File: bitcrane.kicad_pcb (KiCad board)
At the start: 4 copper layers, 110 x 100 mm, 119 parts, among them J1 PSU Comm, J10 Hashboard2, J14 0353180420, J15 0353180420, J16 0353180420, J17 0353180420, J2 Hashboard0, J3 0455580003, J4 61900411021, J5 61900411021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

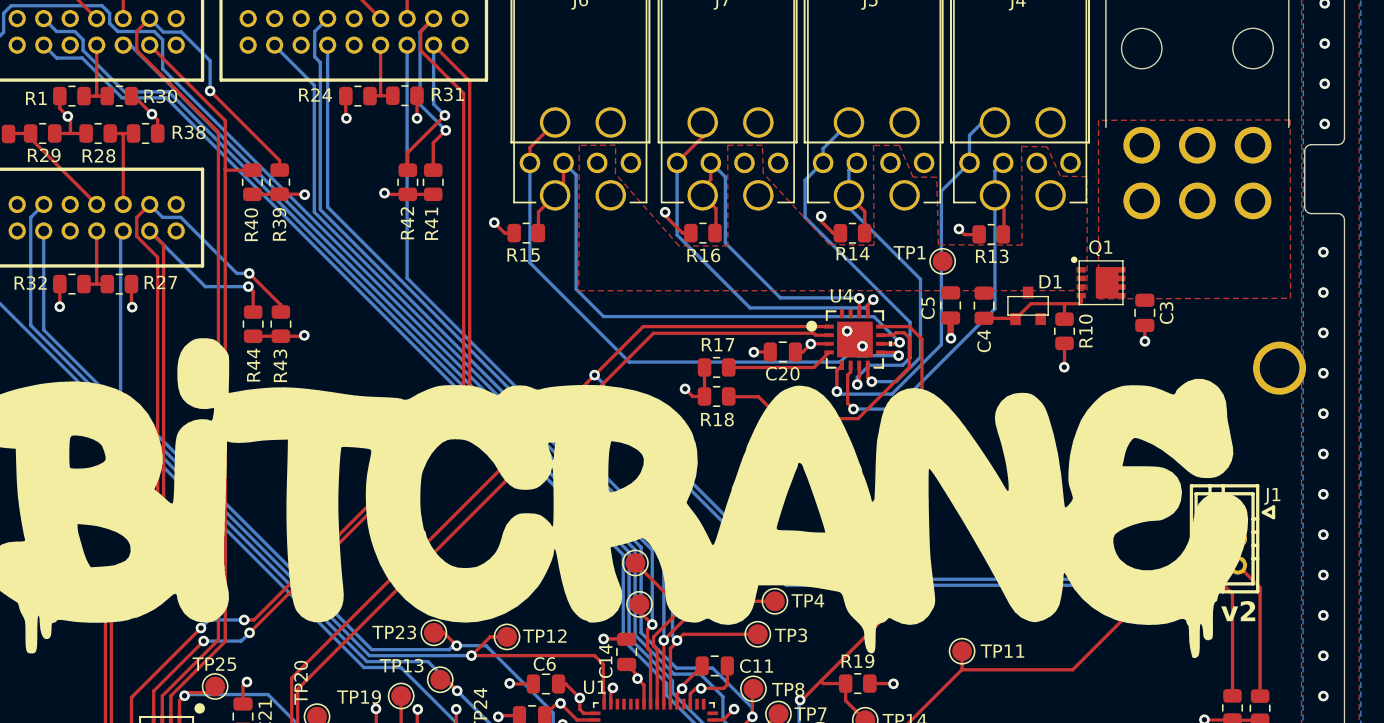
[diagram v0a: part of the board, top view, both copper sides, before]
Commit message: fix for #8. regenerated gerbers. bump version to 2.1
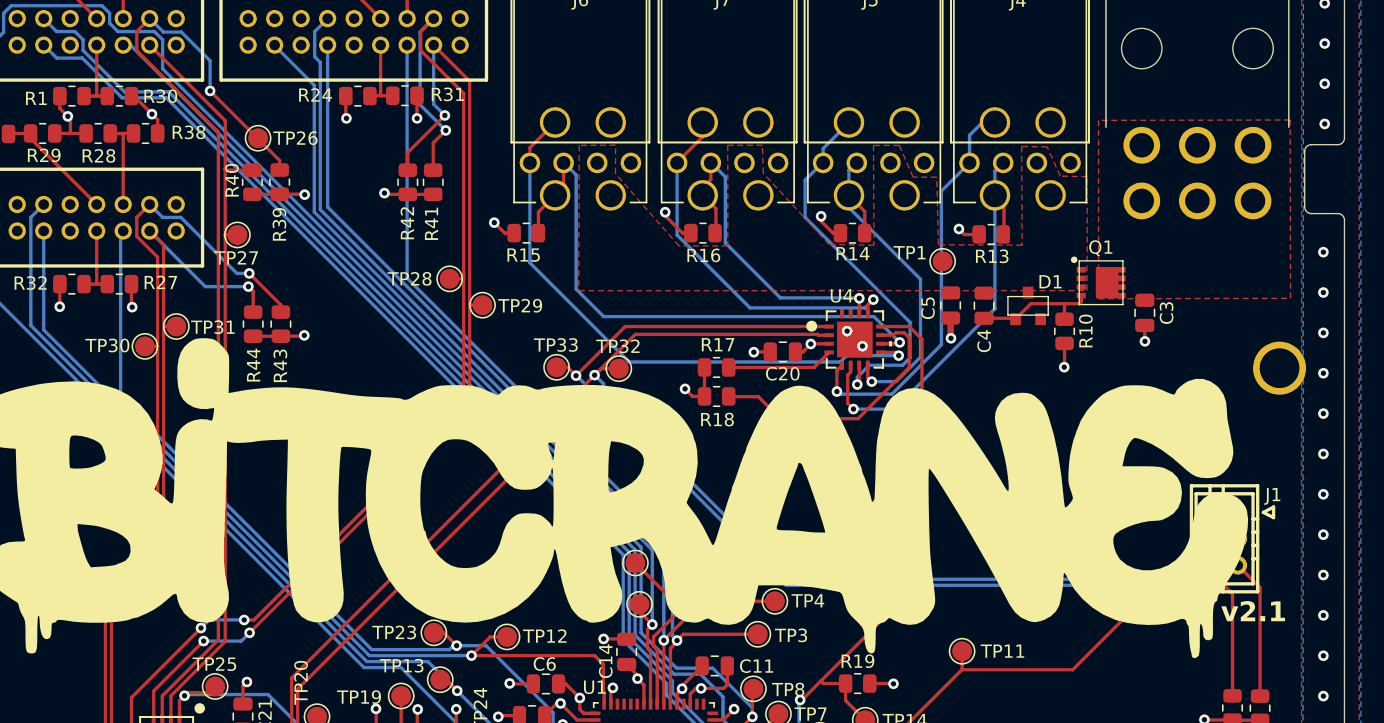
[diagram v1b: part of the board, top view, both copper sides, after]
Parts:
- added TP26: TestPoint, TestPoint:TestPoint_Pad_D1.5mm, F.Cu at (86.3, 50.0)
- added TP27: TestPoint, TestPoint:TestPoint_Pad_D1.5mm, F.Cu at (84.7, 57.3)
- added TP28: TestPoint, TestPoint:TestPoint_Pad_D1.5mm, F.Cu at (100.7, 60.6)
- added TP29: TestPoint, TestPoint:TestPoint_Pad_D1.5mm, F.Cu at (103.2, 62.6)
- added TP30: TestPoint, TestPoint:TestPoint_Pad_D1.5mm, F.Cu at (77.7, 65.7)
- added TP31: TestPoint, TestPoint:TestPoint_Pad_D1.5mm, F.Cu at (80.1, 64.2)
- added TP32: TestPoint, TestPoint:TestPoint_Pad_D1.5mm, F.Cu at (113.5, 67.4)
- added TP33: TestPoint, TestPoint:TestPoint_Pad_D1.5mm, F.Cu at (108.8, 67.3)
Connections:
- U4 pad 1: /SCL3 -> /SDA3
- U4 pad 2: /SDA3 -> /SCL3
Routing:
- net /SDA3: track 137.4 -> 142.0 mm, vias 1 -> 2
- net /SCL3: track 135.4 -> 137.3 mm
- net /SCL1: track 81.5 -> 82.6 mm
- net /SDA1: track 74.5 -> 75.5 mm
- net /SDA2: track 54.3 -> 55.2 mm
- net /SCL2: track 60.0 -> 61.0 mm
- net /SDA0: track 57.0 -> 58.0 mm
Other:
- board text added: "v2.1"
- board text removed: "v2"

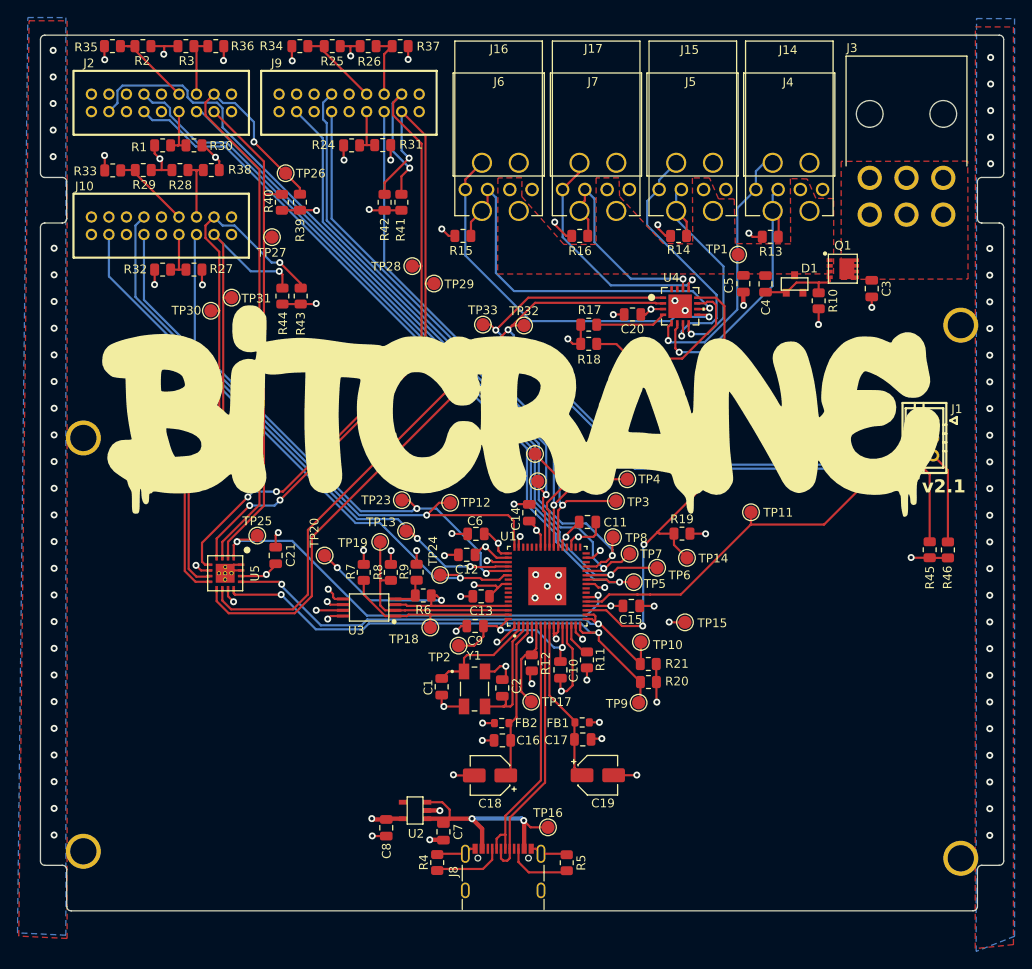
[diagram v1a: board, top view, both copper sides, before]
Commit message: fix for #9. regenerated gerbers. bumped version to 2.2
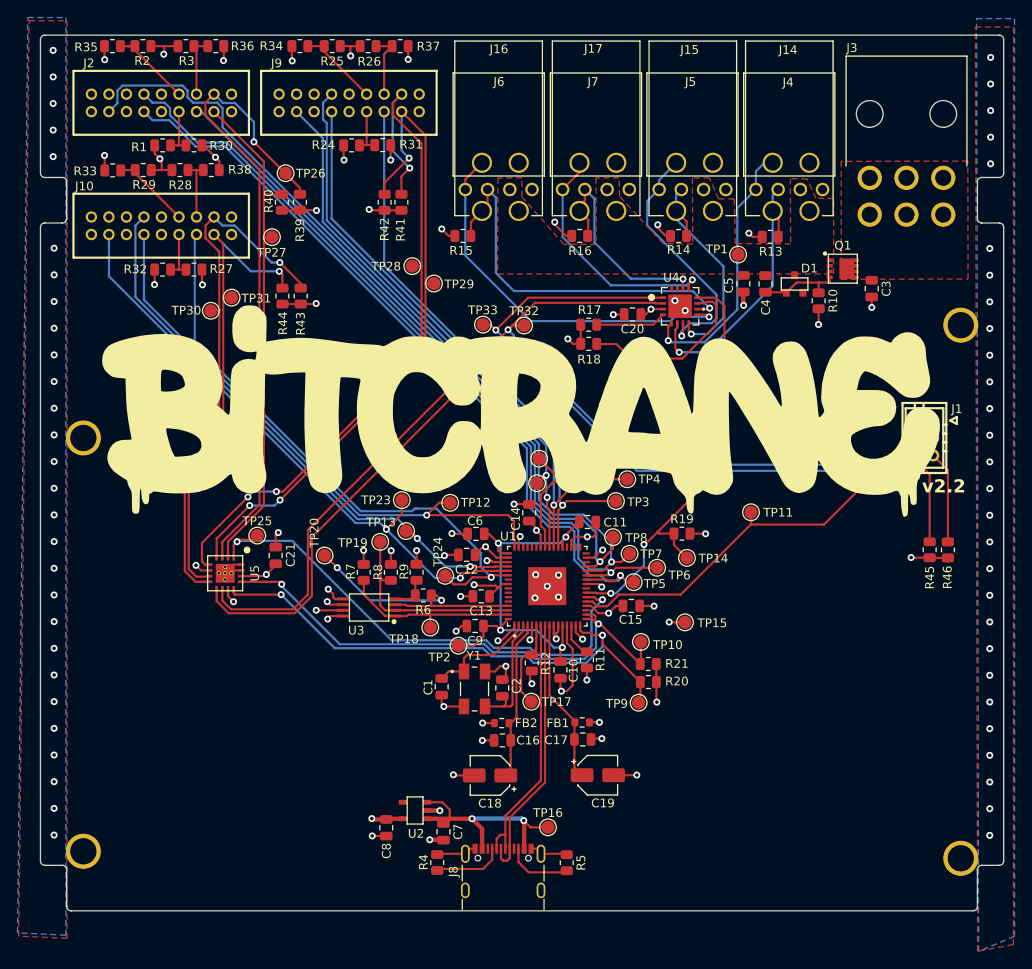
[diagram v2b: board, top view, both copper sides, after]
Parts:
- moved TP21 3.35 mm to (115.0, 85.4)
- moved TP22 2.58 mm to (115.2, 82.6)
- moved TP24 0.59 mm to (104.5, 96.0)
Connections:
- TP21 pad 1: /PLUG1 -> /RST1
- TP22 pad 1: /RST1 -> /PLUG1
- TP23 pad 1: /PLUG2 -> /RST2
- TP24 pad 1: /RST2 -> /PLUG2
- TP7 pad 1: /PLUG0 -> /RST0
- TP8 pad 1: /RST0 -> /PLUG0
- U1 pad 19: /FAN_ALERT -> unconnected-(U1-ADBUS3-Pad19)
- U1 pad 23: unconnected-(U1-ADBUS6-Pad23) -> /FAN_ALERT
- U1 pad 28: /PLUG0 -> /RST0
- U1 pad 29: /RST0 -> /PLUG0
- U1 pad 40: /PLUG1 -> /RST1
- U1 pad 41: /RST1 -> /PLUG1
- U1 pad 53: /PLUG2 -> /RST2
- U1 pad 54: /RST2 -> /PLUG2
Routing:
- net /RESET: track 52.4 -> 58.7 mm
- net /FAN_ALERT: track 56.5 -> 50.3 mm
- net /SDA: track 56.2 -> 60.4 mm
- net /PLUG2: track 62.8 -> 66.8 mm, vias 2 -> 1
- net /SCL: track 57.5 -> 60.9 mm
- net /TXD0: track 86.4 -> 88.8 mm
- net /RST2: track 67.4 -> 69.1 mm, vias 1 -> 2
- net /RXD0: track 89.3 -> 90.6 mm
- net /RST0: track 93.3 -> 94.6 mm
- net VCCIO: track 95.5 -> 96.5 mm
- net GND: track 107.1 -> 106.5 mm
- net /RST1: track 63.7 -> 63.4 mm, vias 1 -> 2
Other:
- board text added: "v2.2"
- board text removed: "v2.1"

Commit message: fix for #10 small DRC fixes. updated to v2.3
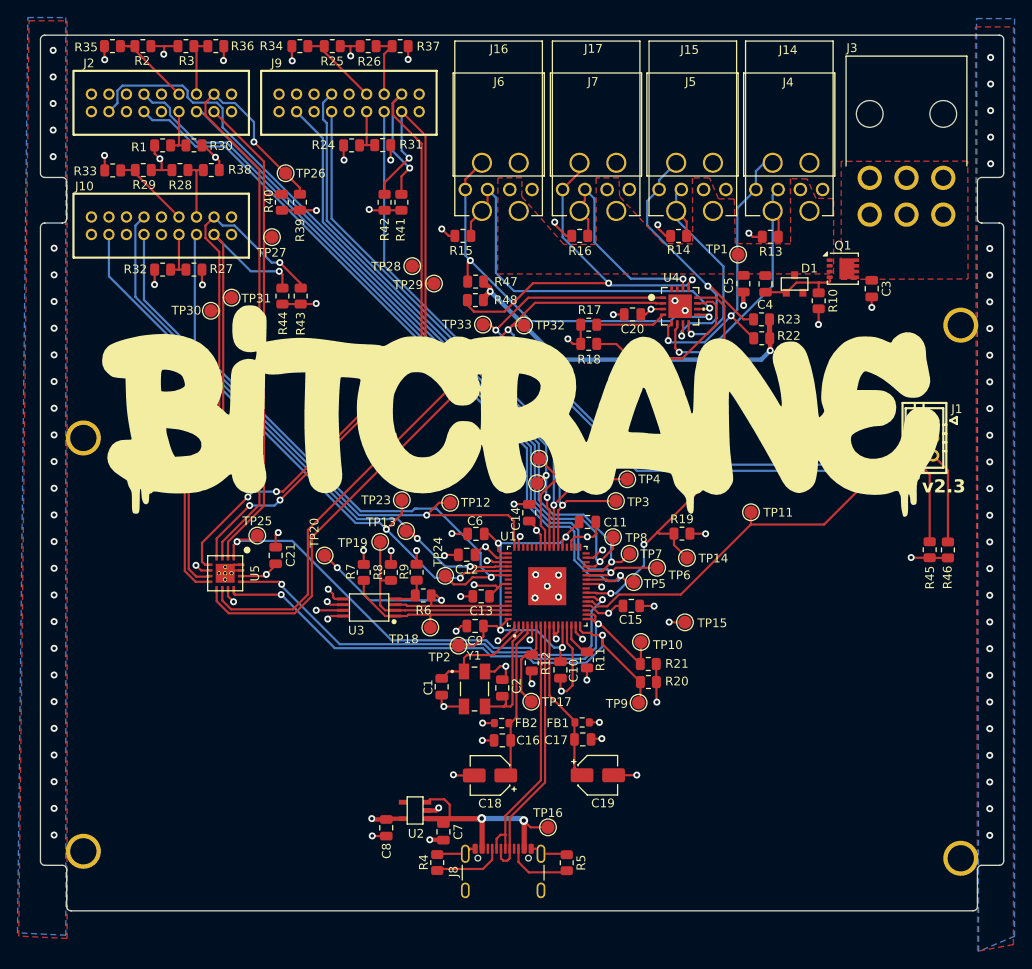
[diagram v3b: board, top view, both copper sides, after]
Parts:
- added R22: 10K, Resistor_SMD:R_0805_2012Metric, F.Cu at (140.6, 68.9)
- added R23: 10K, Resistor_SMD:R_0805_2012Metric, F.Cu at (140.6, 66.7)
- added R47: 10K, Resistor_SMD:R_0805_2012Metric, F.Cu at (108.0, 62.4)
- added R48: 10K, Resistor_SMD:R_0805_2012Metric, F.Cu at (107.9, 64.5)
- turned R6 to 0 degrees
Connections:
- net Net-(J14-Pin_3) renamed /TACH1
- net Net-(J14-Pin_4) renamed /PWM1
- net Net-(J15-Pin_3) renamed /TACH2
- net Net-(J15-Pin_4) renamed /PWM2
- net Net-(J16-Pin_3) renamed /TACH3
- net Net-(J16-Pin_4) renamed /PWM3
- net Net-(J17-Pin_3) renamed /TACH4
- net Net-(J17-Pin_4) renamed /PWM4
- R6 pad 1: Net-(U1-EEDATA) -> Net-(U3-Q)
- R6 pad 2: Net-(U3-Q) -> Net-(U1-EEDATA)
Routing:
- net /5V: track 25.4 -> 140.5 mm, vias 2 -> 4
- net /PWM4: track 27.9 -> 46.2 mm, vias 1 -> 2
- net /PWM2: track 29.0 -> 35.8 mm, vias 1 -> 2
- net /PWM1: track 30.6 -> 34.3 mm, vias 1 -> 2
- net /PWM3: track 44.0 -> 46.5 mm, vias 1 -> 2
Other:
- board text added: "v2.3"
- board text removed: "v2.2"

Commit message: added PCB labels for Fans and Hashboards. Starting to add LCSC part numbers
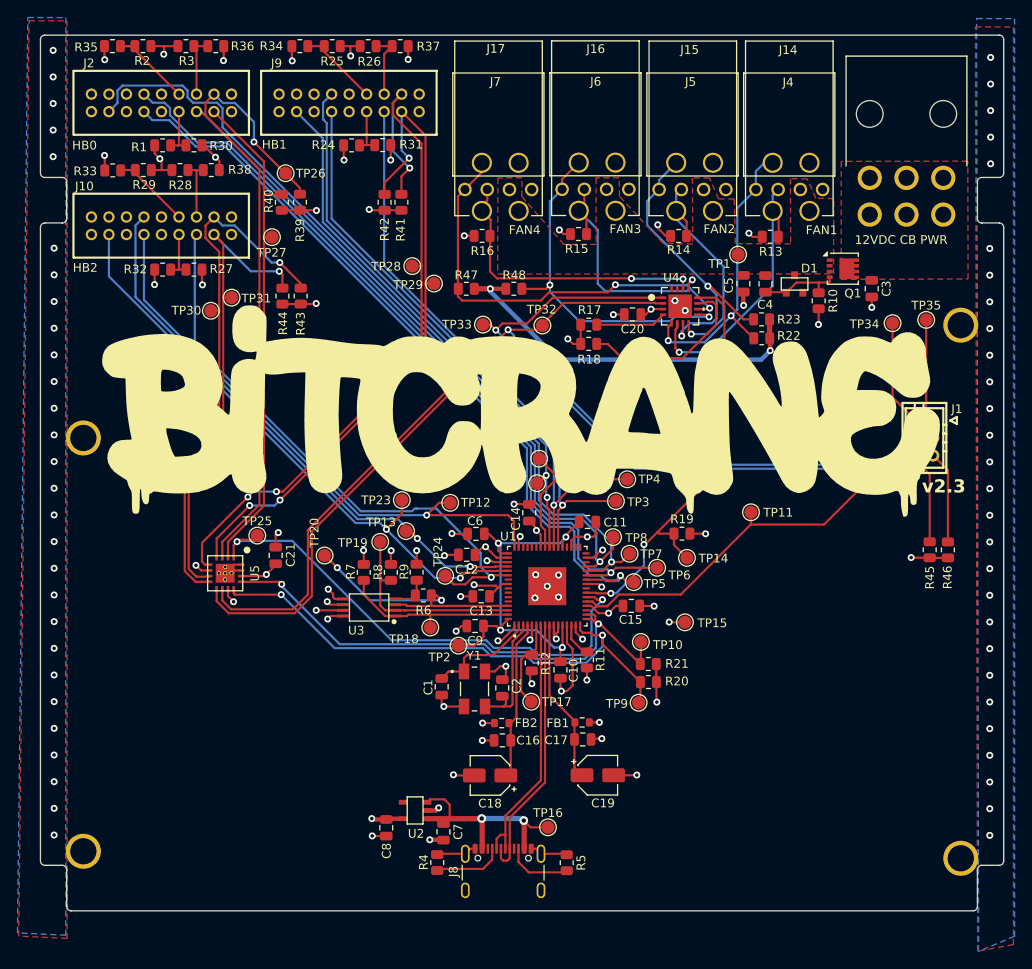
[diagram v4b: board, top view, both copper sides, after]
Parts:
- added TP34: TestPoint, TestPoint:TestPoint_Pad_D1.5mm, F.Cu at (155.6, 67.1)
- added TP35: TestPoint, TestPoint:TestPoint_Pad_D1.5mm, F.Cu at (159.4, 66.8)
- J10: value Hashboard2 -> 2x9P 2mm
- J2: value Hashboard0 -> 2x9P 2mm
- J9: value Hashboard1 -> 2x9P 2mm
- moved R15 13.2 mm to (119.7, 57.0)
- moved J7 11.2 mm to (114.4, 51.9)
- moved R16 11.2 mm to (108.7, 57.2)
- moved J17 11.1 mm to (108.7, 48.8)
- moved J16 11.1 mm to (119.7, 48.8)
- moved J6 11.1 mm to (125.5, 51.9)
- moved R47 4.44 mm to (112.3, 63.2), turned to 180 degrees
- moved TP32 2.09 mm to (115.6, 67.4)
- moved R48 1.66 mm to (106.9, 63.2)
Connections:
- J1 pad 1: unconnected-(J1-Pin_1-Pad1) -> Net-(J1-Pin_1)
- J1 pad 4: unconnected-(J1-Pin_4-Pad4) -> Net-(J1-Pin_4)
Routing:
- net /TACH3: track 43.3 -> 30.4 mm
- net Net-(J1-Pin_4): track 0.00 -> 12.2 mm
- net Net-(J1-Pin_1): track 0.00 -> 11.8 mm
- net /TACH4: track 25.7 -> 33.9 mm, vias 1 -> 2
- net /PWM3: track 46.5 -> 40.7 mm
- net /SCL3: track 137.3 -> 135.2 mm
- net VCCIO: track 96.5 -> 94.5 mm
- net /5V: track 140.5 -> 141.9 mm
- net /PWM4: track 46.2 -> 45.6 mm
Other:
- board text added: "12VDC CB PWR"
- board text added: "FAN1"
- board text added: "FAN2"
- board text added: "FAN3"
- board text added: "FAN4"
- board text added: "HB0"
- board text added: "HB1"
- board text added: "HB2"

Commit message: added almost all LCSC part numbers
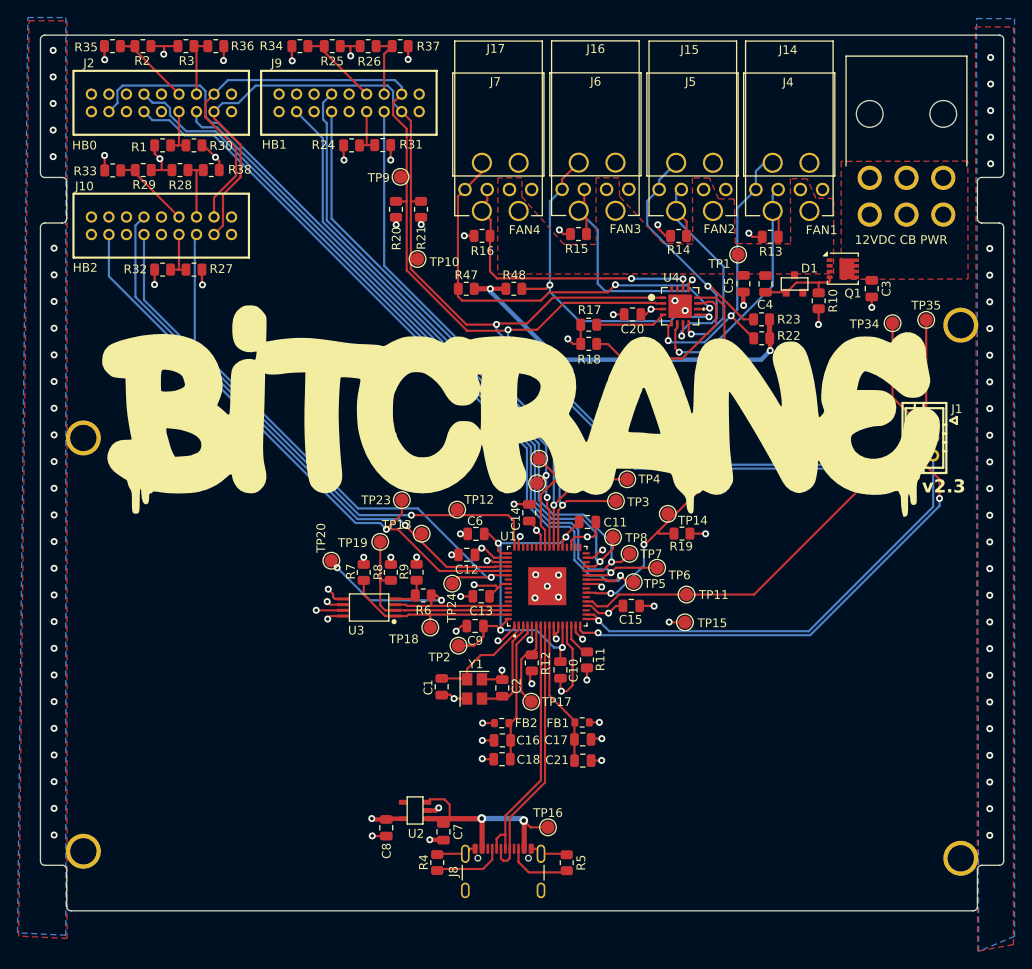
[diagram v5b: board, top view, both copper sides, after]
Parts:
- removed C19: 4.7uF, Capacitor_SMD:CP_Elec_4x5.4
- removed R39, R40, R41, R42, R43, R44, R45, R46: 4.7K, Resistor_SMD:R_0805_2012Metric
- removed TP25, TP26, TP27, TP28, TP29, TP30, TP31, TP32, TP33: TestPoint, TestPoint:TestPoint_Pad_D1.5mm
- removed U5: PCA9546ARGVR, bitcart:QFN-16_EP_4x4_Pitch0.65mm
- C18: value 4.7uF -> 47uF; footprint Capacitor_SMD:CP_Elec_4x5.4 -> Capacitor_SMD:C_0805_2012Metric
- C21: value 0.1uF -> 47uF
- C3: value 0.1uF 100V -> 0.1uF
- D1: value MMBZ5242BLT3G -> LBZX84C12LT1G
- R1, R2, R20, R21, R24, R25, R26, R27, R28, R29, R3, R30, R31, R32, R33, R34, R35, R36, R37, R38: value 4.7K -> 4.7k
- R10, R12: value 12K -> 12k
- R11: value 1K -> 1k
- R13, R14, R15, R16: value 36K -> 36k
- R22, R23, R47, R48, R7, R8, R9: value 10K -> 10k
- R4, R5: value 5.1K -> 5.1k
- R6: value 2.2K -> 2.2k
- Y1: footprint bitcrane:XTAL_405C35B12M00000 -> Crystal:Crystal_SMD_3225-4Pin_3.2x2.5mm
- moved TP9 65.9 mm to (99.4, 50.4)
- moved R20 61.2 mm to (98.9, 54.1), turned to -90 degrees
- moved R21 58.0 mm to (101.7, 54.1), turned to -90 degrees
- moved TP10 50.6 mm to (101.3, 59.8)
- moved C21 42.2 mm to (120.2, 117.1), turned to 0 degrees
- moved TP11 11.9 mm to (132.0, 98.1)
- moved TP14 5.49 mm to (129.9, 88.9)
- moved C18 2.31 mm to (111.0, 116.9)
- moved TP13 1.81 mm to (101.8, 91.2)
- moved TP24 1.20 mm to (105.3, 96.9)
- moved TP12 1.12 mm to (105.8, 88.4)
- moved TP20 0.97 mm to (91.5, 94.3)
- turned Y1 to -90 degrees
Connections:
- C21 pad 1: VCCIO -> Net-(U1-VPLL)
- J1 pad 3: /SDA3 -> /SDA
- J1 pad 6: /SCL3 -> /SCL
- J10 pad 3: /SDA2 -> /SDA
- J10 pad 4: /SCL2 -> /SCL
- J2 pad 3: /SDA0 -> /SDA
- J2 pad 4: /SCL0 -> /SCL
- J9 pad 3: /SDA1 -> /SDA
- J9 pad 4: /SCL1 -> /SCL
- U1 pad 22: /RESET -> unconnected-(U1-ADBUS5-Pad22)
- U4 pad 1: /SDA3 -> /SDA
- U4 pad 2: /SCL3 -> /SCL
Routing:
- net /SDA: track 60.4 -> 205.2 mm
- net /SCL: track 60.9 -> 205.3 mm, vias 2 -> 3
- net /SDA3: track 142.4 -> 0.00 mm, vias 2 -> 0
- net /SCL3: track 135.2 -> 0.00 mm, vias 1 -> 0
- net /SCL1: track 82.6 -> 0.00 mm, vias 3 -> 0
- net /SDA1: track 75.5 -> 0.00 mm, vias 3 -> 0
- net /SCL0: track 73.9 -> 0.00 mm, vias 1 -> 0
- net /SCL2: track 61.0 -> 0.00 mm, vias 1 -> 0
- net /RESET: track 58.7 -> 0.00 mm, vias 2 -> 0
- net /SDA0: track 58.0 -> 0.00 mm
- net /SDA2: track 55.2 -> 0.00 mm, vias 1 -> 0
- net VCCIO: track 94.5 -> 69.0 mm, vias 36 -> 32
- net GND: track 106.5 -> 93.1 mm, vias 102 -> 99
- net /FAN_ALERT: track 50.3 -> 46.9 mm
- net /TXD2: track 66.5 -> 63.2 mm
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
